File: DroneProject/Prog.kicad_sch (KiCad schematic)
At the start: 17 parts, among them SW131 TS02CBE, U131 NC7SZ04P5X, U132 TS3A4751PWR, U133 SN74LVC1G08DBVR, U134 TS3A4751PWR, U135 SN74LVC1G08DBVR, U136 TS3A4751PWR

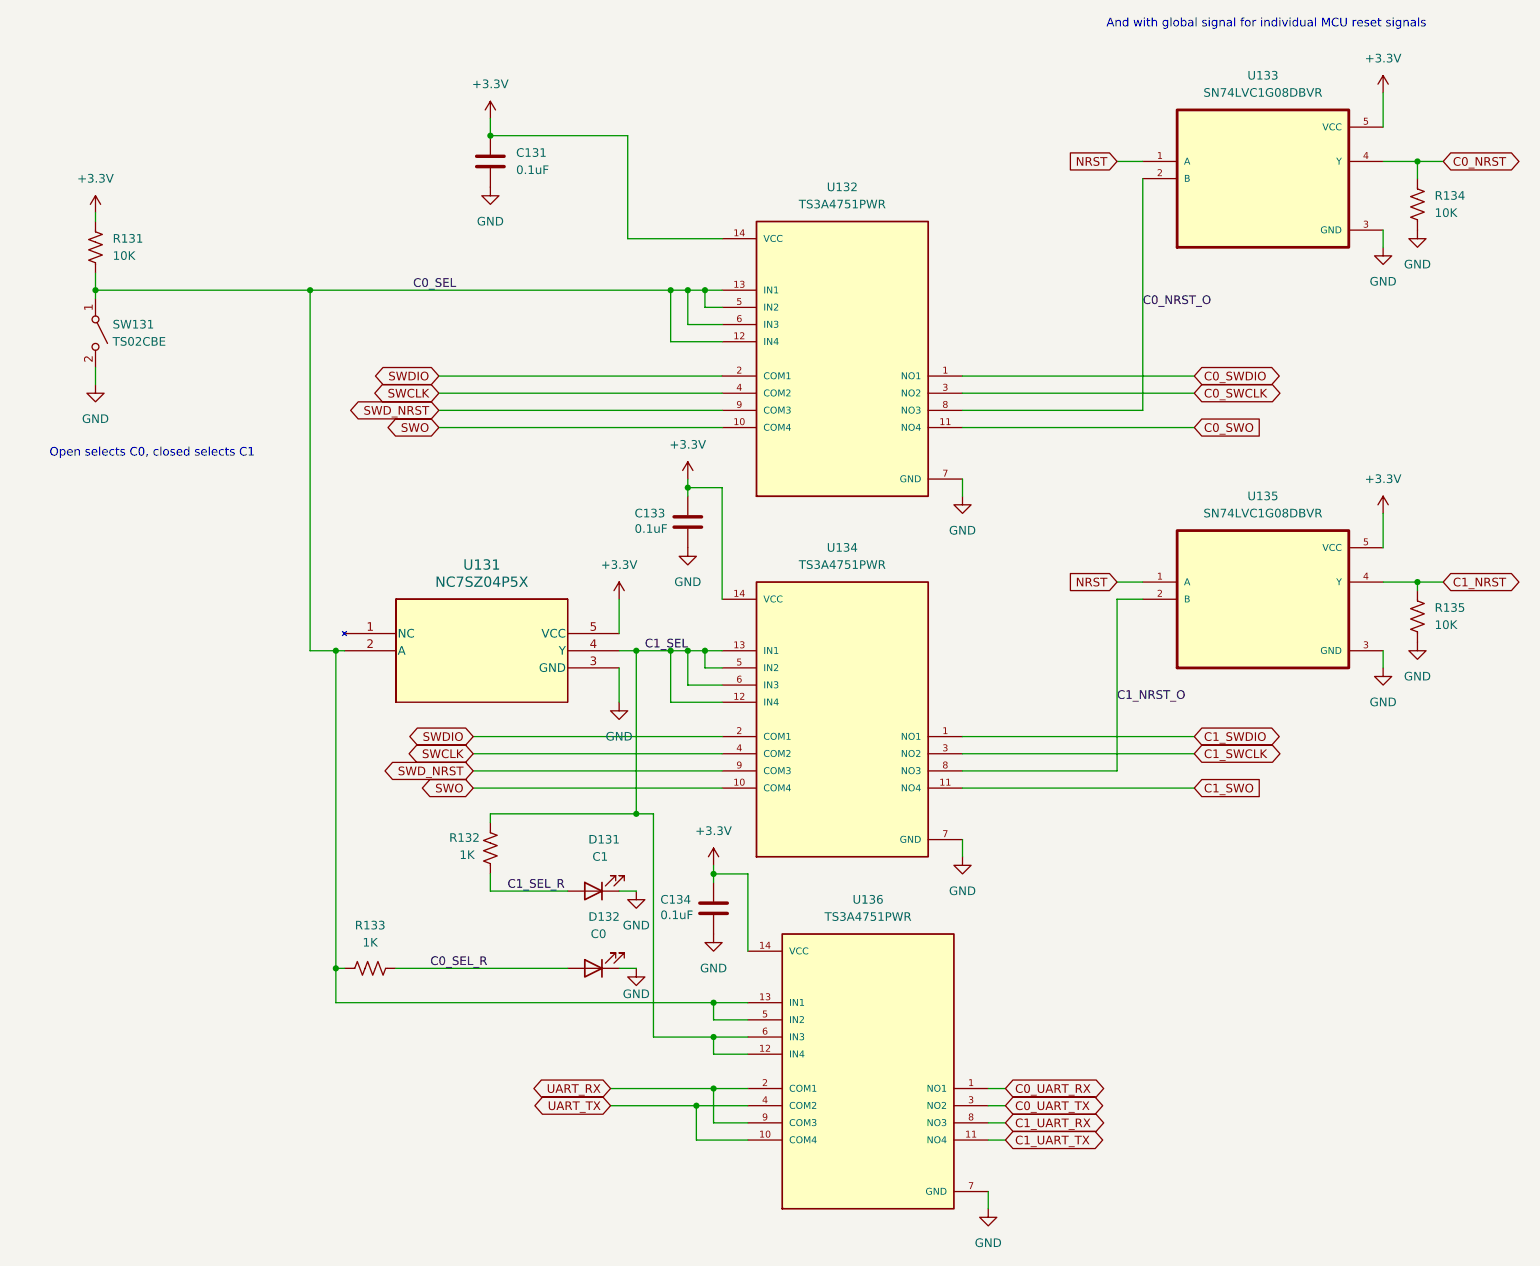
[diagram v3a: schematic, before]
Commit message: Removed C1 and motor controllers from main platform and moved to own project
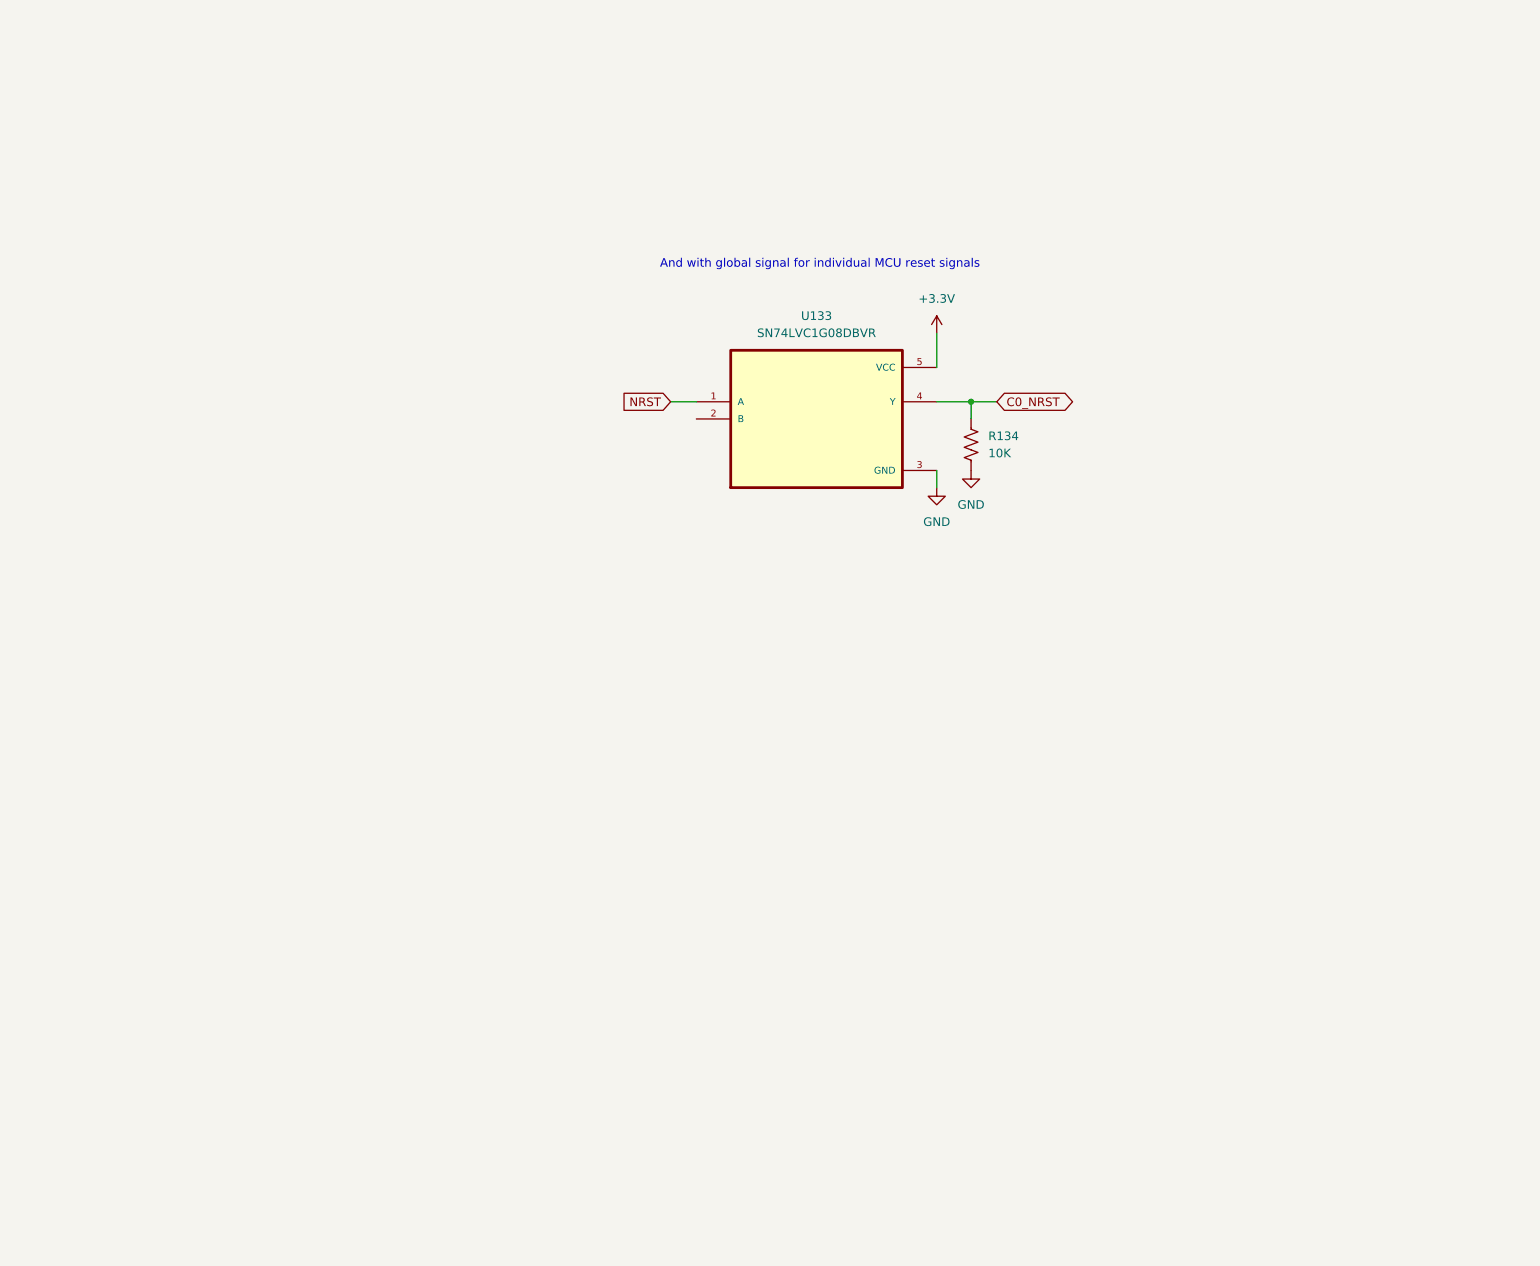
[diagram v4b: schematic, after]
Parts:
- removed C131, C133, C134: 0.1uF, Capacitor_SMD:C_0402_1005Metric, symbol Device:C
- removed D131: C1, LED_SMD:LED_0603_1608Metric, symbol Device:LED
- removed D132: C0, LED_SMD:LED_0603_1608Metric, symbol Device:LED
- removed R131, R135: 10K, Resistor_SMD:R_0402_1005Metric, symbol Device:R_US
- removed R132, R133: 1K, Resistor_SMD:R_0402_1005Metric, symbol Device:R_US
- removed SW131: TS02CBE, Library:SW_TS02_10P16X5P08_CNK, symbol Switch:SW_SPST
- removed U131: NC7SZ04P5X, SC-88A-5_1P35X2P2_ONS, symbol Global:NC7SZ04P5X
- removed U132, U134, U136: TS3A4751PWR, Library:SOP65P640X120-14N, symbol Global:TS3A4751PWR
- removed U135: SN74LVC1G08DBVR, Library:SOT95P280X145-5N, symbol Global:SN74LVC1G08DBVR
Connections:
- net C0_NRST_O: no longer names the net of U133.2 (B)
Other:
- note removed: "Open selects C0, closed selects C1"
- moved on the sheet: R134, U133
